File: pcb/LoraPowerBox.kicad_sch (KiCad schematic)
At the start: 48 parts, among them J1 Conn_01x04_Pin, J10 Conn_01x02_Pin, J11 Conn_01x02_Pin, J12 Conn_01x05_Pin, J2 Conn_01x04_Pin, J3 Conn_01x04_Pin, J4 Conn_01x06_Pin, J5 Conn_01x04_Pin, J6 Conn_01x04_Pin, J7 Conn_01x04_Pin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

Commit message: pcb, sch: expose interrupt pin of charge controller to test pad
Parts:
- added TP1: TestPoint, TestPoint:TestPoint_Pad_D1.0mm, symbol Connector:TestPoint
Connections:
- net at U2.11 (INTn): now also TP1.1
- no-connect marks 5 -> 4
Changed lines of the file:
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@@
 		(color 0 0 0 0)
 	)
-	(junction
-		(at 191.77 125.73)
-		(diameter 0)
-		(color 0 0 0 0)
-	)
-	(no_connect
-		(at 120.65 156.21)
-	)
 	(no_connect
 		(at 147.32 165.1)
@@
 	(wire
 		(pts
-			(xy 191.77 124.46) (xy 191.77 125.73)
-		)
-		(stroke
-			(width 0)
-			(type default)
-		)
-	)
-	(wire
-		(pts
 			(xy 76.2 243.84) (xy 77.47 243.84)
 		)
@@
 	(wire
 		(pts
-			(xy 191.77 125.73) (xy 196.85 125.73)
+			(xy 182.88 125.73) (xy 196.85 125.73)
 		)
 		(stroke
@@
 	(wire
 		(pts
-			(xy 182.88 125.73) (xy 191.77 125.73)
-		)
-		(stroke
-			(width 0)
-			(type default)
-		)
-	)
-	(wire
-		(pts
 			(xy 25.4 173.99) (xy 34.29 173.99)
 		)
@@
 	(wire
 		(pts
+			(xy 110.49 156.21) (xy 120.65 156.21)
+		)
+		(stroke
+			(width 0)
+			(type default)
+		)
+	)
+	(wire
+		(pts
 			(xy 96.52 49.53) (xy 101.6 49.53)
 		)
@@
 	(wire
 		(pts
+			(xy 110.49 156.21) (xy 110.49 162.56)
+		)
+		(stroke
+			(width 0)
+			(type default)
+		)
+	)
+	(wire
+		(pts
 			(xy 163.83 167.64) (xy 163.83 166.37)
 		)
@@
 		)
 	)
-	(label "VMID"
-		(at 179.07 125.73 0)
-		(effects
-			(font
-				(size 1.27 1.27)
-			)
-			(justify left bottom)
-		)
-	)
 	(label "I2C1_SCL"
 		(at 60.96 170.18 270)
@@
 		(dnp no)
 		(property "Reference" "D3"
-			(at 97.536 162.306 90)
+			(at 104.648 160.274 90)
 			(effects
 				(font
@@
 		)
 		(property "Value" "LED"
-			(at 99.06 162.56 0)
+			(at 105.41 166.116 0)
 			(effects
 				(font
@@
 	)
 	(symbol
+		(lib_id "Connector:TestPoint")
+		(at 110.49 162.56 180)
+		(unit 1)
+		(exclude_from_sim no)
+		(in_bom yes)
+		(on_board yes)
+		(dnp no)
+		(property "Reference" "TP1"
+			(at 109.474 168.148 0)
+			(effects
+				(font
+					(size 1.27 1.27)
+				)
+				(justify right)
+			)
+		)
+		(property "Value" "TestPoint"
+			(at 113.03 167.1319 0)
+			(effects
+				(font
+					(size 1.27 1.27)
+				)
+				(justify right)
+				(hide yes)
+			)
+		)
+		(property "Footprint" "TestPoint:TestPoint_Pad_D1.0mm"
+			(at 105.41 162.56 0)
+			(effects
+				(font
+					(size 1.27 1.27)
+				)
+				(hide yes)
+			)
+		)
+		(property "Datasheet" "~"
+			(at 105.41 162.56 0)
+			(effects
+				(font
+					(size 1.27 1.27)
+				)
+				(hide yes)
+			)
+		)
+		(property "Description" "test point"
+			(at 110.49 162.56 0)
+			(effects
+				(font
+					(size 1.27 1.27)
+				)
+				(hide yes)
+			)
+		)
+		(pin "1"
+		)
+		(instances
+			(project ""
+				(path "/25fca8d1-9891-46d7-9368-b9fbe57cc258"
+					(reference "TP1")
+					(unit 1)
+				)
+			)
+		)
+	)
+	(symbol
 		(lib_id "Device:L")
 		(at 227.33 106.68 90)
@@
 		(dnp no)
 		(property "Reference" "D2"
-			(at 93.472 162.814 90)
+			(at 98.044 160.782 90)
 			(effects
 				(font
@@
 		)
 		(property "Value" "LED"
-			(at 95.25 162.56 0)
+			(at 99.06 166.624 0)
 			(effects
 				(font

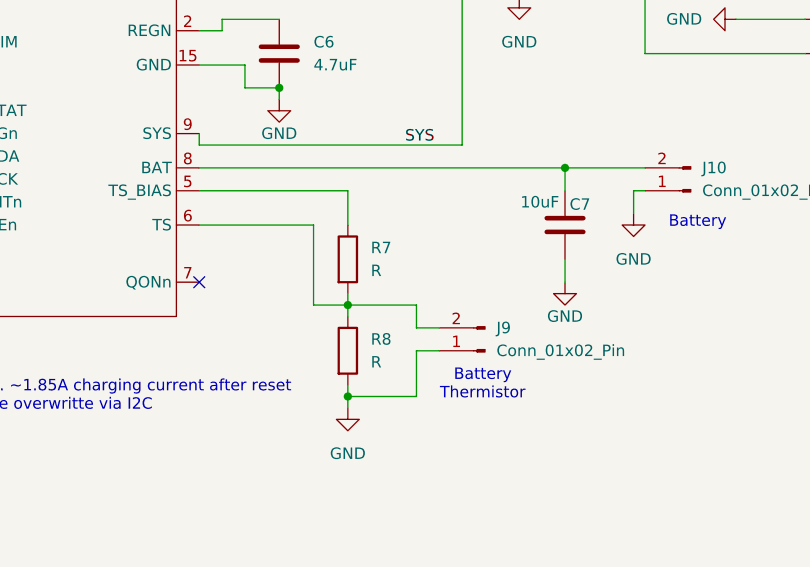
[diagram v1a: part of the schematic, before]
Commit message: pcb, sch: add resistor values for NTC voltage divider
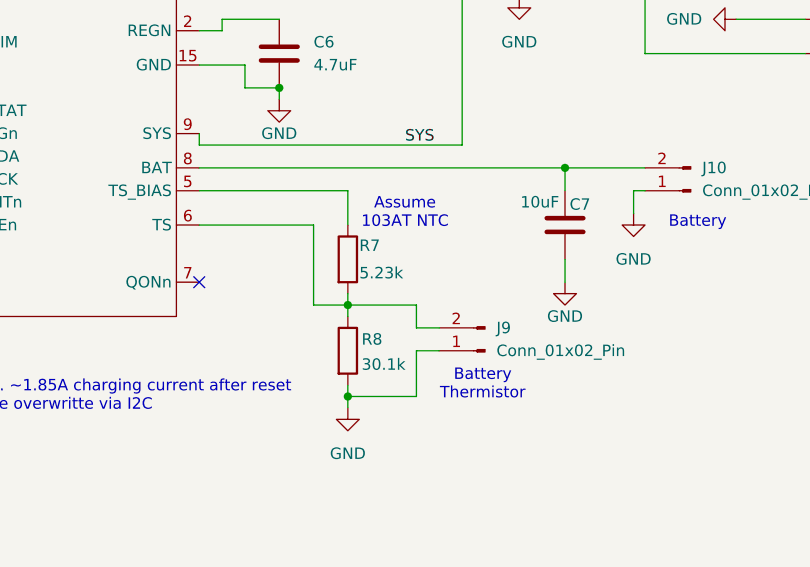
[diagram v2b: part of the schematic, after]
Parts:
- R7: value R -> 5.23k
- R8: value R -> 30.1k
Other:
- note added: "Assume 103AT NTC"
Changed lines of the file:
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@@
 		)
 	)
+	(text "Assume \n103AT NTC"
+		(exclude_from_sim no)
+		(at 170.18 157.48 0)
+		(effects
+			(font
+				(size 1.27 1.27)
+			)
+		)
+	)
 	(text "Battery\n"
 		(exclude_from_sim no)
@@
 		(on_board yes)
 		(dnp no)
-		(fields_autoplaced yes)
 		(property "Reference" "R7"
-			(at 166.37 161.2899 0)
+			(at 165.1 161.036 0)
 			(effects
 				(font
@@
 			)
 		)
-		(property "Value" "R"
-			(at 166.37 163.8299 0)
+		(property "Value" "5.23k"
+			(at 165.1 164.084 0)
 			(effects
 				(font
@@
 		(on_board yes)
 		(dnp no)
-		(fields_autoplaced yes)
 		(property "Reference" "R8"
-			(at 166.37 171.4499 0)
+			(at 165.354 171.45 0)
 			(effects
 				(font
@@
 			)
 		)
-		(property "Value" "R"
-			(at 166.37 173.9899 0)
+		(property "Value" "30.1k"
+			(at 165.354 174.244 0)
 			(effects
 				(font

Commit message: pcb, sch: replace M3 hounting hole with M4
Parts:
- H1: footprint MountingHole:MountingHole_3.2mm_M3 -> MountingHole:MountingHole_4.3mm_M4_DIN965
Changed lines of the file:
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@@
 			)
 		)
-		(property "Footprint" "MountingHole:MountingHole_3.2mm_M3"
+		(property "Footprint" "MountingHole:MountingHole_4.3mm_M4_DIN965"
 			(at 167.64 278.13 0)
 			(effects

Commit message: sch, pcb: add reset IC that monitors the battery for us
The BQ25628 has a UVLO (Battery Undervoltage Lockout) protection which
is very very low (configurable voltages <2.5).

Add an additional battery monitor which allows us to automatically
switch off the 3.3V coming from the Buck-/Boost-Converter but keeps the
BQ25628 alive so it can recharge the battery.
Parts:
- added C13: 100nF, Capacitor_SMD:C_0603_1608Metric_Pad1.08x0.95mm_HandSolder, symbol Device:C
- added R13: 100k, Capacitor_SMD:C_0603_1608Metric_Pad1.08x0.95mm_HandSolder, symbol Device:R
- added U4: APX803L05, Package_TO_SOT_SMD:SOT-23_Handsoldering, symbol library:APX803L05
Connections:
- net GND: now also C13.1, U4.1 (GND)
- net SYS: no longer U3.5 (EN)
- net VBAT: now reaches C7.2, J10.2 (Pin_2), U2.8 (BAT)
- net VBAT: now also C13.2, R13.2, U4.3 (VCC)
- new net: R13.1, U3.5 (EN), U4.2 (RESETn)
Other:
- note added: "With a APX803L05-29SA-7 we can hard switch-off the entire payload to protect the battery from deep discharge. In this case at 2.9V battery voltage."

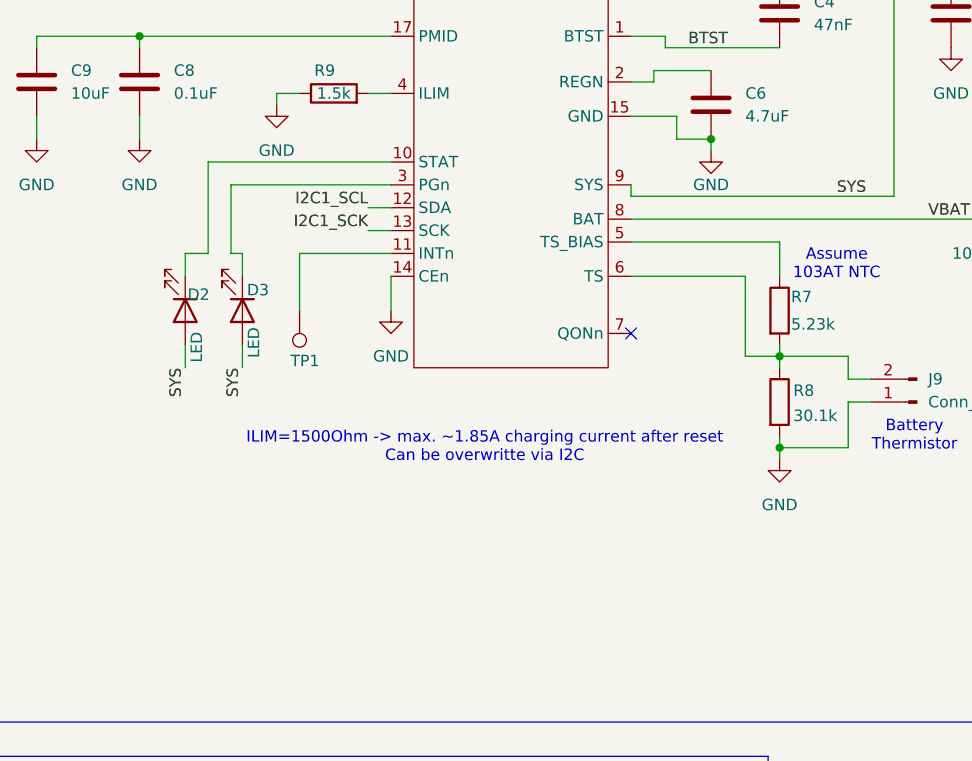
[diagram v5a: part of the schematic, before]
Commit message: pcb, sch: add a resistor to the LEDs
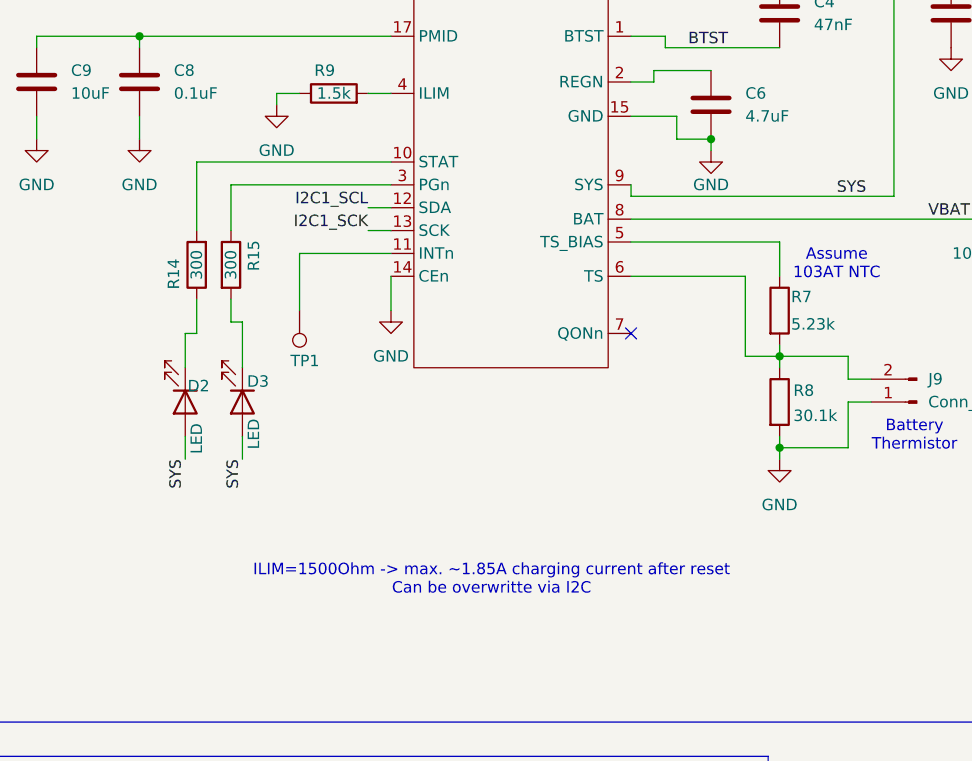
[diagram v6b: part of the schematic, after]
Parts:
- added R14, R15: 300, Resistor_SMD:R_0603_1608Metric_Pad0.98x0.95mm_HandSolder, symbol Device:R
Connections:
- net at U2.10 (STAT): now also R14.2; no longer D2.1 (K)
- net at U2.3 (PGn): now also R15.1; no longer D3.1 (K)
- new net: D3.1 (K), R15.2
- new net: D2.1 (K), R14.1
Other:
- moved on the sheet: D2, D3
